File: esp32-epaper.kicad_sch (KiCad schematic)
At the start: 46 parts, among them J1 USB-C 16P, J2 FPC-26P 0.5mm, Q1 AO3400A, SW1 SW SPDT, U1 ESP32-WROOM-32D, U2 SSD1680, U3 TP4056, U4 DW01A, U5 FS8205A, U6 HT7333-1

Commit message: fix: KiCad 7 schematic validation - lib_symbols complete + ERC pass
- Added 7 missing standard KiCad library symbol definitions (Device:C/R/D/L/LED/Q_NMOS, RF_Module:ESP32-WROOM-32D)
- Fixed global_label shape types (power_out/power_in -> output/input) for KiCad 7 compatibility
- Fixed version string to 20221206 for KiCad 7.0.x
- Netlist export: 46 components, 186 nets
- PDF export verified
- Added helper scripts: fix_lib_symbols.py, test_elements.py
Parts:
- BT1, C16, C17, C2, C6, D5, D6, D7, D8, J1, Q1, SW1, U2, U3, U4, U5, U6: now in the parts list
- C1, C19, C20, C3, C4, C5: value 10µF -> 10uF; now in the parts list
- C10, C11, C12, C13, C14, C15, C7, C8, C9: value 1µF -> 1uF; now in the parts list
- C18: value 4.7µF -> 4.7uF; now in the parts list
- J2: value FPC-26P 0.5mm -> FPC-26P; now in the parts list
- L1: value 68µH -> 68uH; now in the parts list
- R1, R2, R3, R7: value 10kΩ -> 10kohm; now in the parts list
- R10, R9: value 5.1kΩ -> 5.1kohm; now in the parts list
- R11: value 1kΩ -> 1kohm; now in the parts list
- R4: value 1.2kΩ -> 1.2kohm; now in the parts list
- R5: value 100Ω -> 100ohm; now in the parts list
- R8: value 0.47Ω -> 0.47ohm; now in the parts list
- U1: footprint (none) -> RF_Module:ESP32-WROOM-32D; now in the parts list
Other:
- note added: "C: Power Management"
- note removed: "C: Power Management (USB-C → TP4056 → DW01A → HT7333)"

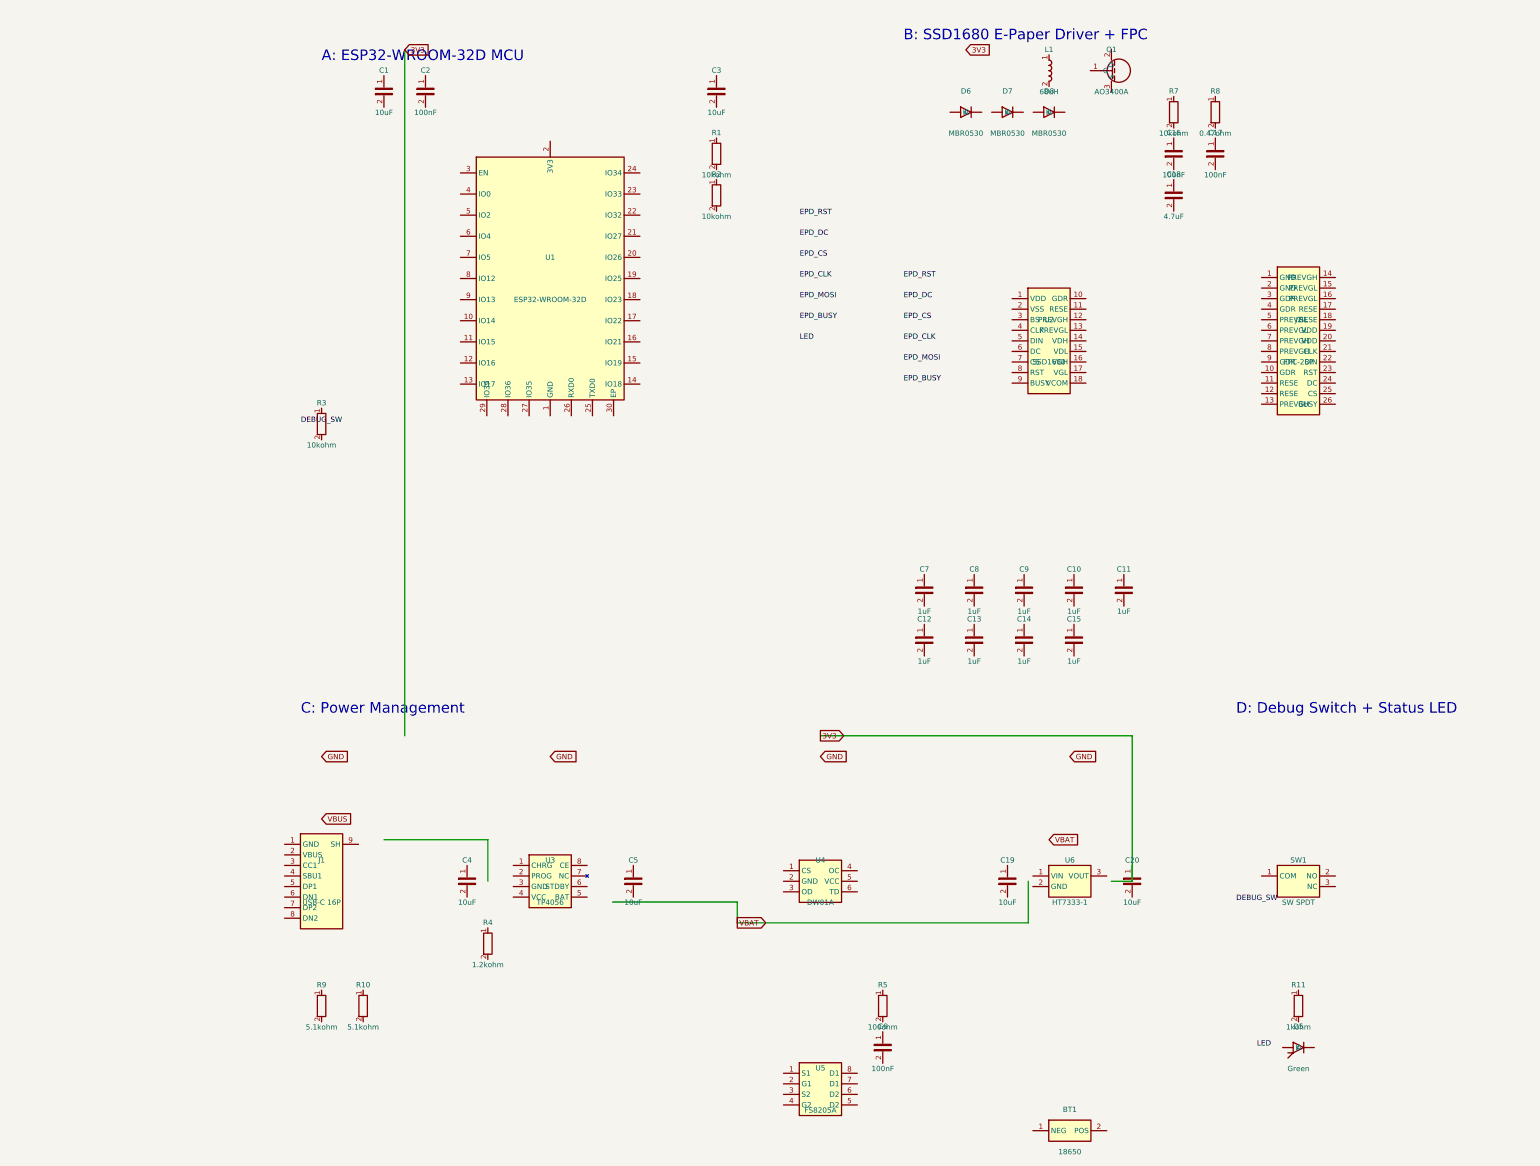
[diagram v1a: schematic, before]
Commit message: feat: add battery voltage sensing divider (R12/R13/C21)
New components:
- R12 (100k): BAT+ to VBAT_SENSE divider top
- R13 (100k): VBAT_SENSE to GND divider bottom
- C21 (100nF): VBAT_SENSE filter cap to GND
- GPIO34 (ADC1_CH6) assigned as VBAT_SENSE

Design review:
- Divider ratio 1:1, max sense voltage 2.1V (< 3.6V ADC range)
- Static current 21uA, annual battery impact < 5%
- Cutoff freq ~32Hz (adequate for DC measurement)
- BOM delta: +3 parts, +0.04 yuan

KiCad 7 validation: 49 components, netlist+PDF export pass
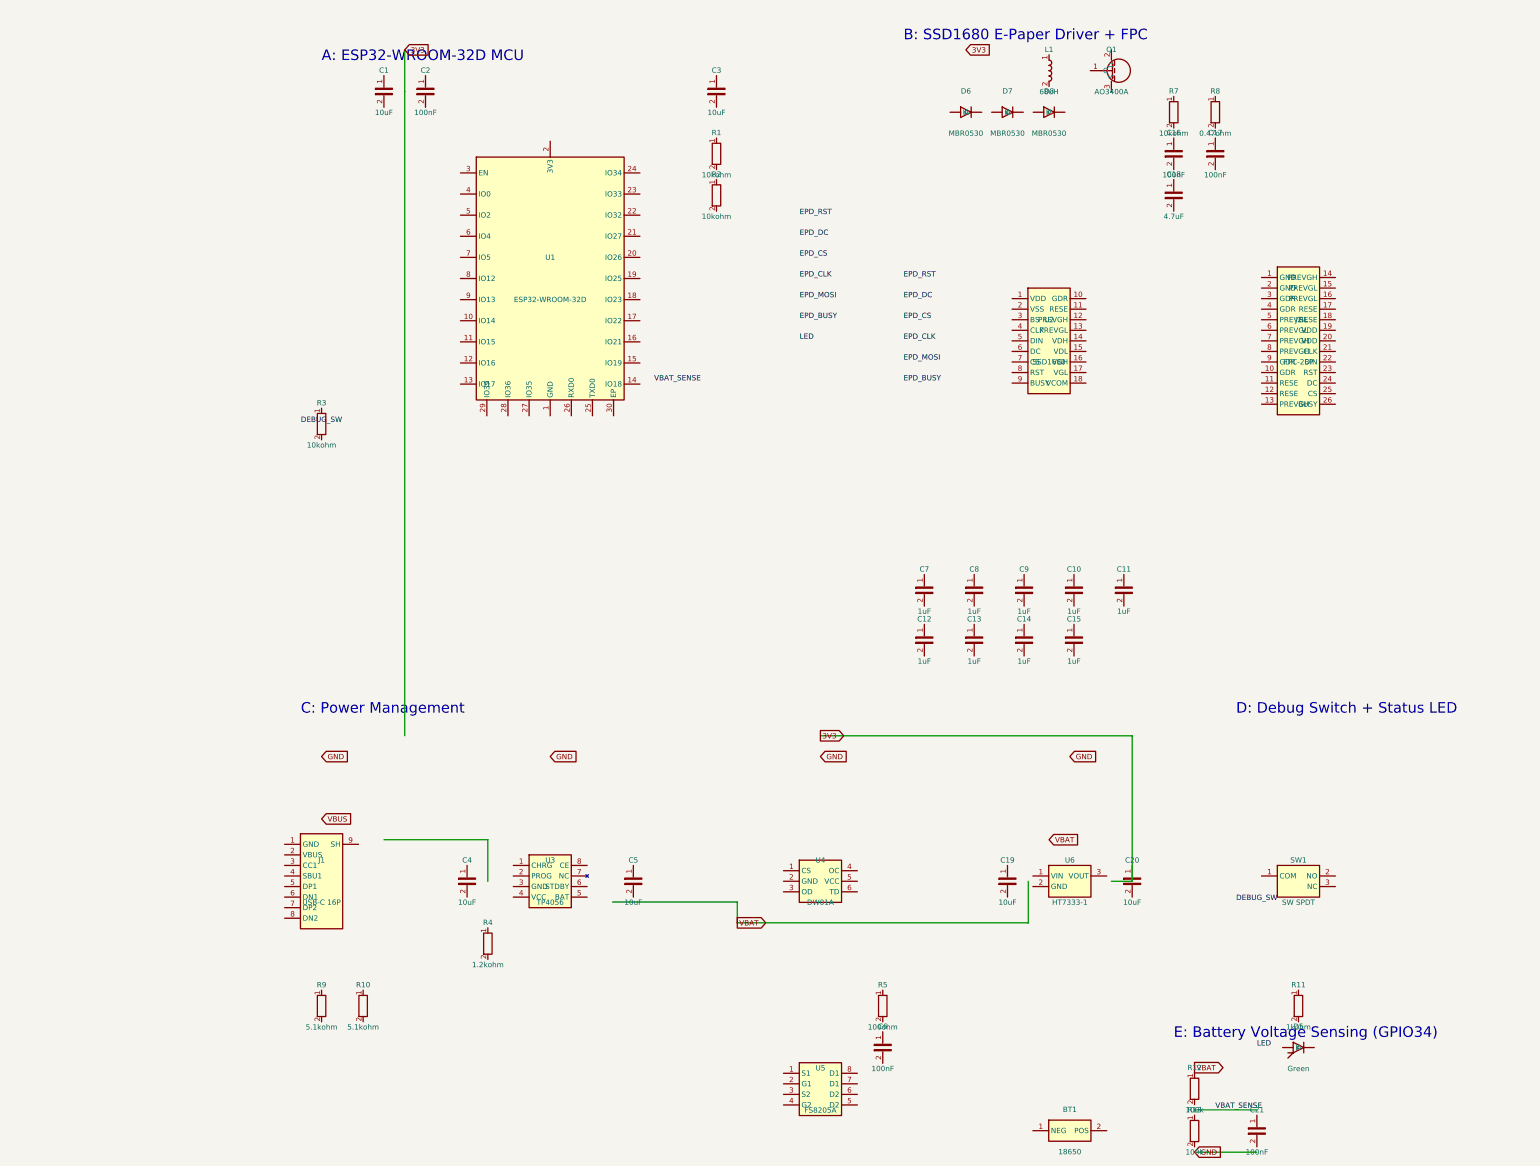
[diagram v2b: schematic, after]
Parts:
- added C21: 100nF, symbol Device:C
- added R12, R13: 100k, symbol Device:R
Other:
- note added: "E: Battery Voltage Sensing (GPIO34)"
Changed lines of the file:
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@@
     (comment 2 "2.13\" Tri-color E-Paper, USB-C Charging")
+  )
+  (text "E: Battery Voltage Sensing (GPIO34)" (at 225 248 0)
+    (effects (font (size 2.54 2.54)) (justify left bottom))
   )
   (text "A: ESP32-WROOM-32D MCU" (at 20 13 0)
@@
     (effects (font (size 2.54 2.54)) (justify left bottom))
   )
+  (wire (pts (xy 230 265.0) (xy 245 265.0))
+    (stroke (width 0) (type default))
+  )
+  (wire (pts (xy 230 275.16) (xy 245 275.16))
+    (stroke (width 0) (type default))
+  )
   (wire (pts (xy 35 200) (xy 60 200))
     (stroke (width 0) (type default))
@@
   (wire (pts (xy 40 10) (xy 40 20))
     (stroke (width 0) (type default))
+  )
+  (global_label "VBAT" (shape output) (at 230 254.84 0) (fields_autoplaced)
+    (effects (font (size 1.27 1.27)) (justify left))
+  )
+  (label "VBAT_SENSE" (at 235 265.0 0)
+    (effects (font (size 1.27 1.27)) (justify left bottom))
+  )
+  (global_label "GND" (shape input) (at 230 275.16 0) (fields_autoplaced)
+    (effects (font (size 1.27 1.27)) (justify left))
+  )
+  (label "VBAT_SENSE" (at 100 90 0)
+    (effects (font (size 1.27 1.27)) (justify left bottom))
   )
   (global_label "VBUS" (shape input) (at 20 195 0) (fields_autoplaced)
@@
     )
   )
+  (symbol (lib_id "Device:R") (at 230 259.92 0) (unit 1)
+    (in_bom yes) (on_board yes) (dnp no)
+    (property "Reference" "R12" (at 230 254.84 0)
+      (effects (font (size 1.27 1.27)))
+    )
+    (property "Value" "100k" (at 230 265.0 0)
+      (effects (font (size 1.27 1.27)))
+    )
+    (pin "1")
+    (pin "2")
+    (instances
+      (project "esp32-epaper"
+        (path "/6281fcfa-6553-4706-b287-236232e6465c"
+          (reference "R12") (unit 1)
+        )
+      )
+    )
+  )
+  (symbol (lib_id "Device:R") (at 230 270.08 0) (unit 1)
+    (in_bom yes) (on_board yes) (dnp no)
+    (property "Reference" "R13" (at 230 265.0 0)
+      (effects (font (size 1.27 1.27)))
+    )
+    (property "Value" "100k" (at 230 275.15999999999997 0)
+      (effects (font (size 1.27 1.27)))
+    )
+    (pin "1")
+    (pin "2")
+    (instances
+      (project "esp32-epaper"
+        (path "/6281fcfa-6553-4706-b287-236232e6465c"
+          (reference "R13") (unit 1)
+        )
+      )
+    )
+  )
+  (symbol (lib_id "Device:C") (at 245 270.08 0) (unit 1)
+    (in_bom yes) (on_board yes) (dnp no)
+    (property "Reference" "C21" (at 245 265.0 0)
+      (effects (font (size 1.27 1.27)))
+    )
+    (property "Value" "100nF" (at 245 275.15999999999997 0)
+      (effects (font (size 1.27 1.27)))
+    )
+    (pin "1")
+    (pin "2")
+    (instances
+      (project "esp32-epaper"
+        (path "/6281fcfa-6553-4706-b287-236232e6465c"
+          (reference "C21") (unit 1)
+        )
+      )
+    )
+  )
   (sheet_instances
     (path "/" (page "1"))
   )
   (symbol_instances
+    (path "/6281fcfa-6553-4706-b287-236232e6465c/54a7cd7b-874f-4a66-ba55-5686449b3f6c" (reference "R12") (unit 1) (value "100k") (footprint ""))
+    (path "/6281fcfa-6553-4706-b287-236232e6465c/06daef87-462d-45ee-8b88-b0b52aab98b7" (reference "R13") (unit 1) (value "100k") (footprint ""))
+    (path "/6281fcfa-6553-4706-b287-236232e6465c/41b2fce2-821a-467a-8146-ab040659ef65" (reference "C21") (unit 1) (value "100nF") (footprint ""))
     (path "/6281fcfa-6553-4706-b287-236232e6465c/6402d9dd-a208-4367-8163-666c8787e4f2" (reference "U1") (unit 1) (value "ESP32-WROOM-32D") (footprint "RF_Module:ESP32-WROOM-32D"))
     (path "/6281fcfa-6553-4706-b287-236232e6465c/10cec9ef-4cef-4535-8a27-95e354456df5" (reference "C1") (unit 1) (value "10uF") (footprint ""))
